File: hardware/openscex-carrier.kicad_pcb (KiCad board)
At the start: 2 copper layers, 39.5 x 36.5 mm, 20 parts, among them J1 ISP, Q1 2N3904, SW1 CTS 206-2ST, U1 ATtiny85-20PU

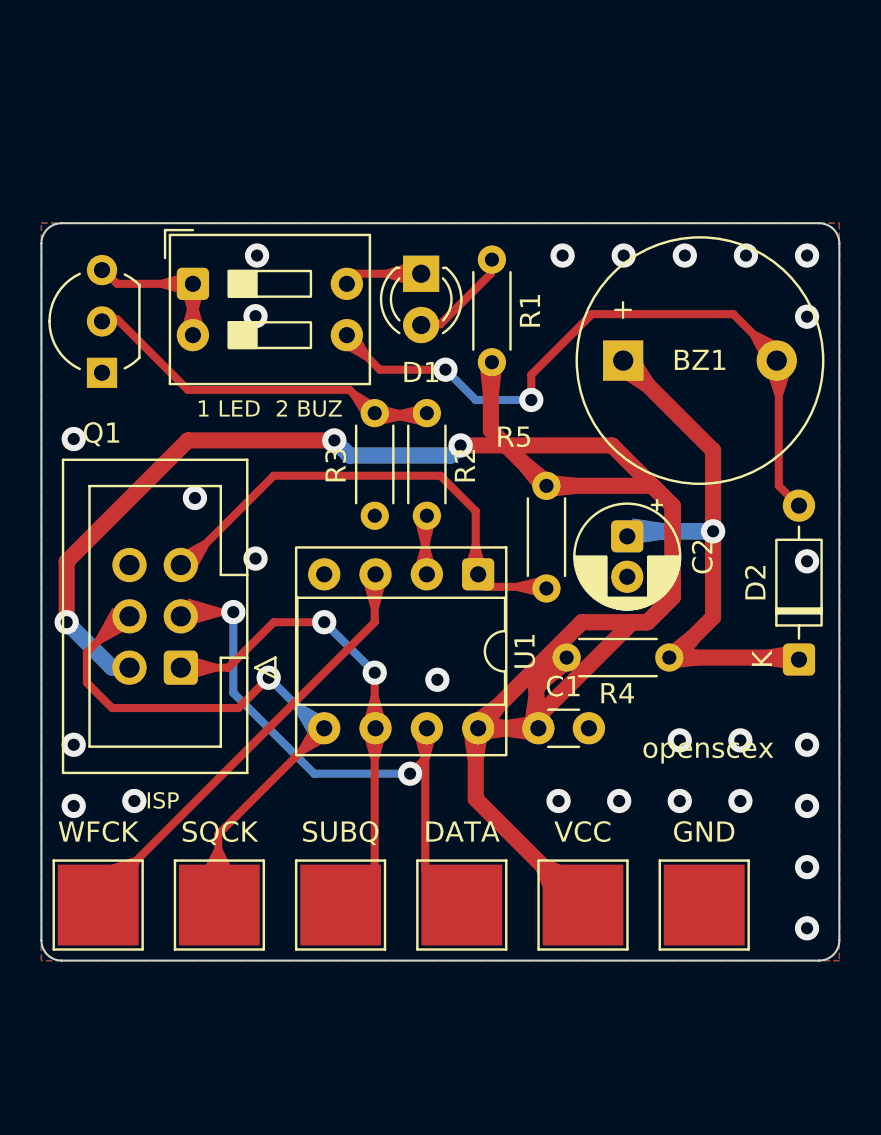
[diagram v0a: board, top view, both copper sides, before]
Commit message: test(hardware): check every board ships its BOM
Each KiCad project in hardware/ must have a bill of materials that
lists exactly the schematic's parts, with matching quantities, and a
Gerber and drill archive holding every layer a board house needs.
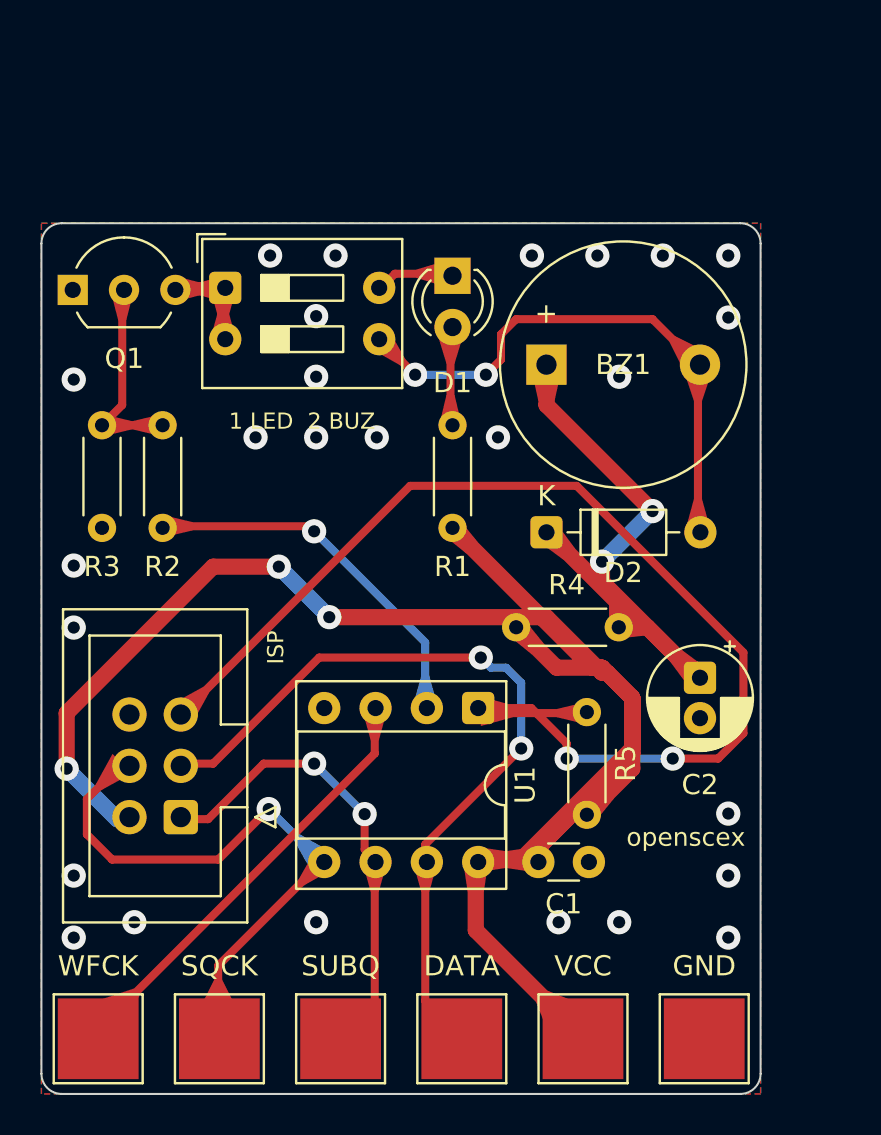
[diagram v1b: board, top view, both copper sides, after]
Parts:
- moved D2 14.0 mm to (123.0, 115.3), turned to 0 degrees
- moved R3 13.5 mm to (101.0, 110.0)
- moved R2 13.1 mm to (104.0, 115.1)
- moved R1 8.43 mm to (118.3, 110.0)
- moved C2 7.87 mm to (130.6, 122.5)
- moved J1 7.40 mm to (104.9, 129.4)
- moved C1 6.62 mm to (122.6, 131.6)
- moved TP1 6.62 mm to (100.8, 140.4)
- moved TP2 6.62 mm to (106.8, 140.4)
- moved TP3 6.62 mm to (112.8, 140.4)
- moved TP4 6.62 mm to (118.8, 140.4)
- moved TP5 6.62 mm to (124.8, 140.4)
- moved TP6 6.62 mm to (130.8, 140.4)
- moved U1 6.62 mm to (119.6, 124.0)
- moved R5 6.44 mm to (125.0, 124.2), turned to -90 degrees
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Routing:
- net /RST: track 24.0 -> 60.7 mm, vias 0 -> 2
- net /PB3: track 3.00 -> 18.6 mm, vias 0 -> 1
- net /DATA: track 29.0 -> 39.6 mm
- net /Q_B: track 18.0 -> 10.2 mm
- net /BUZ_N: track 33.9 -> 27.5 mm
- net /VCC: track 104.2 -> 107.0 mm
- net /Q_C: track 7.31 -> 4.75 mm
- net /VIND: track 32.9 -> 31.9 mm, vias 1 -> 2
- net /SQCK: track 29.1 -> 29.7 mm
- net /SUBQ: track 23.7 -> 23.1 mm
- net /LED_A: track 5.29 -> 4.75 mm
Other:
- board size 39.5 x 36.5 mm -> 35.6 x 43.1 mm

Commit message: feat(hardware): name datasheet-checked parts
Every BOM line now names an exact manufacturer part, each checked
against its own datasheet: Microchip ATTINY85-20PU in a TE
1-2199298-2 socket, KEMET C315C104K5R5TA, Panasonic EEU-FC1A101S,
Vishay MBA0204 resistors, onsemi 2N3904RLRAG and 1N4148TR,
Kingbright WP710A10ID, CTS 206-2ST, Same Sky CMI-1295IC-0385T and
Wurth 61200621621.

C1 moves to a 4.0 x 2.5 mm footprint that fits the KEMET body. A
project footprint library, hardware/openscex.pretty, carries the hole
sizes the Wurth header and the buzzer datasheets recommend, 1.1 mm and
0.8 mm in 2 mm pads.
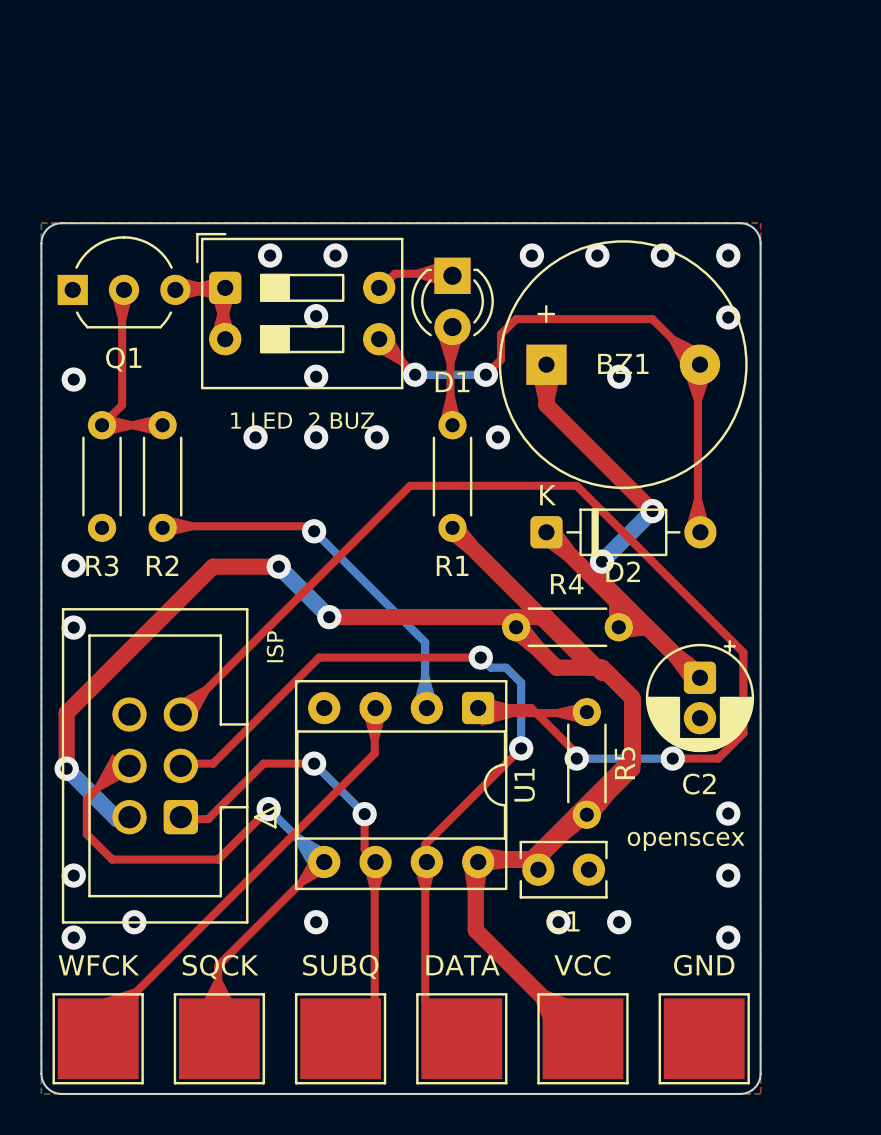
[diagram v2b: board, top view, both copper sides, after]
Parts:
- BZ1: footprint Buzzer_Beeper:Buzzer_12x9.5RM7.6 -> openscex:Buzzer_12x9.5RM7.6_CMI-1295IC-0385T
- C1: footprint Capacitor_THT:C_Disc_D3.0mm_W1.6mm_P2.50mm -> Capacitor_THT:C_Rect_L4.0mm_W2.5mm_P2.50mm
- J1: footprint Connector_IDC:IDC-Header_2x03_P2.54mm_Vertical -> openscex:IDC-Header_2x03_P2.54mm_Vertical_Wurth_61200621621
- moved C1 0.38 mm to (122.6, 132.0)
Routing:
- net /VCC: track 107.0 -> 108.2 mm

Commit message: feat(hardware): add a serial trace header
The carrier gains a band along its top edge for the trace profile: J2,
a 1x6 header in the FTDI TTL-232R pinout with only GND and the cable's
RXD wired, a C&K OS102011MS2QN1 slide switch that hands PB3 to the
indicator or to the header, and 1 kOhm in series with the serial line.
The lower board keeps the mini and bare layout and width.

C1's 3D model is scaled to the KEMET C315 body on all three boards; the
library model is a 10 mm film box.

The READMEs no longer say fat boards run at about 5 V: every board runs
its logic from +3.5 V, and the 5 V rail is not a chip supply.
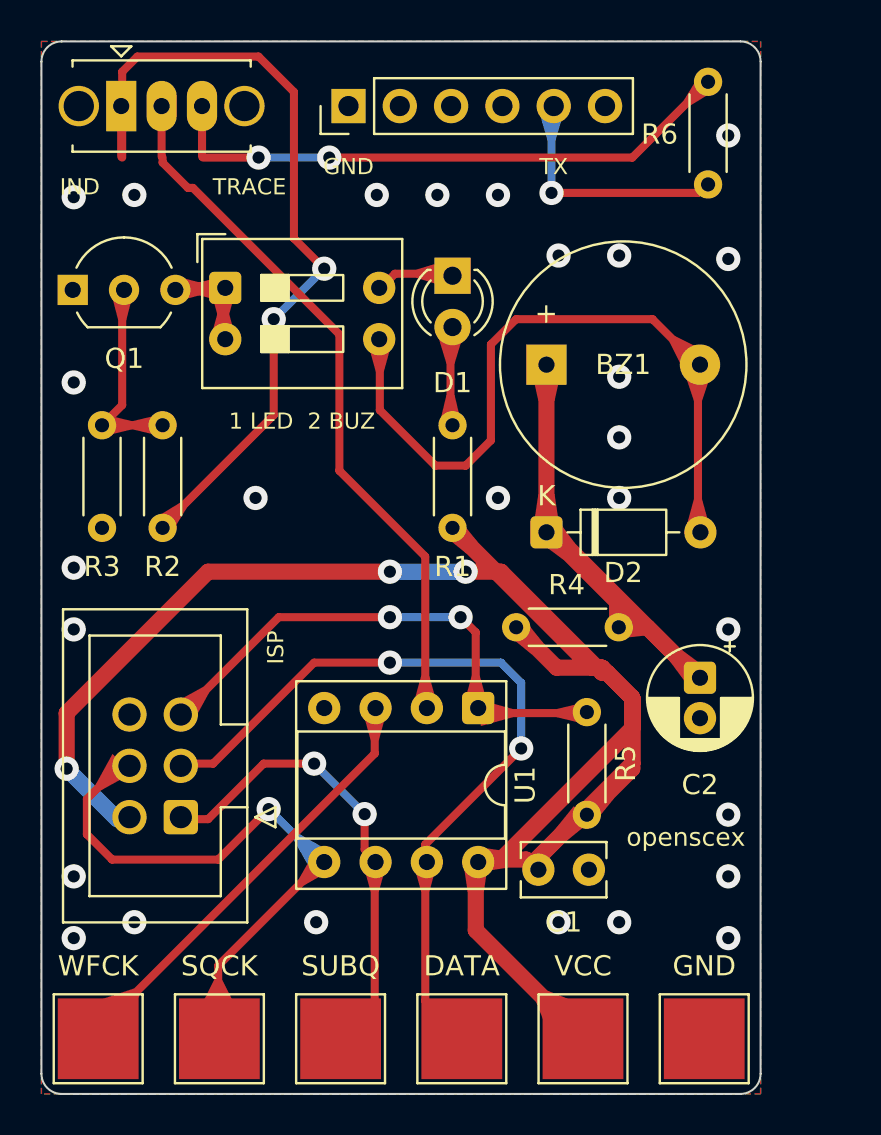
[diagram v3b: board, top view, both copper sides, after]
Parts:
- added J2: TRACE, Connector_PinHeader_2.54mm:PinHeader_1x06_P2.54mm_Vertical, F.Cu at (113.2, 94.2)
- added R6: 1k, Resistor_THT:R_Axial_DIN0204_L3.6mm_D1.6mm_P5.08mm_Horizontal, F.Cu at (131.0, 93.0)
- added SW2: OS102011MS2QN1, openscex:SW_Slide_SPDT_Straight_CK_OS102011MS2Q, F.Cu at (102.0, 94.2)
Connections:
- R2 pad 1: /PB3 -> /IND
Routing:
- net /IND: track 0.00 -> 41.7 mm, vias 0 -> 2
- net /RST: track 60.4 -> 26.1 mm
- net /TRACE: track 0.00 -> 29.1 mm, vias 0 -> 2
- net /PB3: track 18.6 -> 35.3 mm, vias 1 -> 0
- net /TX: track 0.00 -> 12.2 mm, vias 0 -> 1
- net /BUZ_N: track 27.5 -> 35.4 mm, vias 2 -> 0
- net /VIND: track 31.9 -> 29.8 mm, vias 2 -> 0
- net /VCC: track 108.2 -> 107.2 mm
- net /GND: vias 26 -> 27
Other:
- board size 35.6 x 43.1 mm -> 35.6 x 52.1 mm
- board text added: "IND"
- board text added: "TRACE"
- board text added: "TX"
